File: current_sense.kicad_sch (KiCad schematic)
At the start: 6 parts, among them U7 INA241A2IDDFR

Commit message: Start layout
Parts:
- U7: footprint rflib:SOT65P280X110-8N -> footprints:SOT65P280X110-8N
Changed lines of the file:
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@@
 			)
 		)
-		(property "Footprint" "rflib:SOT65P280X110-8N"
+		(property "Footprint" "footprints:SOT65P280X110-8N"
 			(at 167.64 106.68 0)
 			(effects

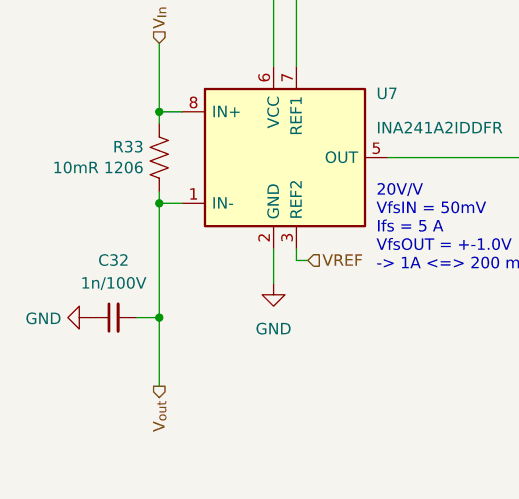
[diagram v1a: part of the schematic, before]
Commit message: Manufacturing update + inductor fix
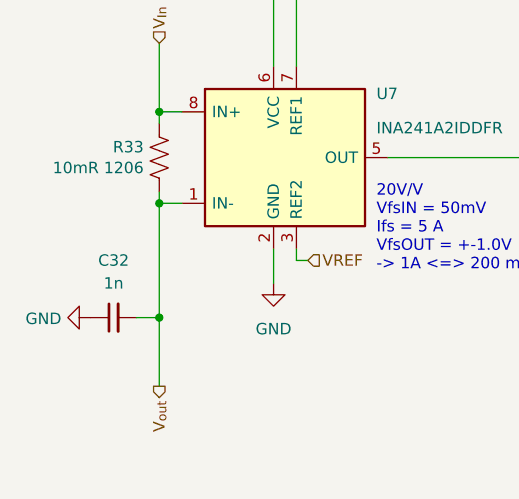
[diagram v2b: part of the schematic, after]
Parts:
- C32: value 1n/100V -> 1n; LCSC C153291 -> C1588
- TP8: LCSC C5199804 -> (none)
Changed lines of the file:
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@@
-			)
-		)
-		(property "LCSC" "C5199804"
-			(at 181.61 107.95 0)
-			(effects
-				(font
-					(size 1.27 1.27)
-				)
-				(hide yes)
 			)
 		)
@@
 			)
 		)
-		(property "Value" "1n/100V"
+		(property "Value" "1n"
 			(at 123.1963 123.19 90)
 			(effects
@@
 			)
 		)
-		(property "LCSC" "C153291"
+		(property "LCSC" "C1588"
 			(at 123.19 127 0)
 			(effects
